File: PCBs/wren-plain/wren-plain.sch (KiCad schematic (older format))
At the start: 68 parts, among them J1 TRRS_Jack, SW0 Reset, U1 Elite-C

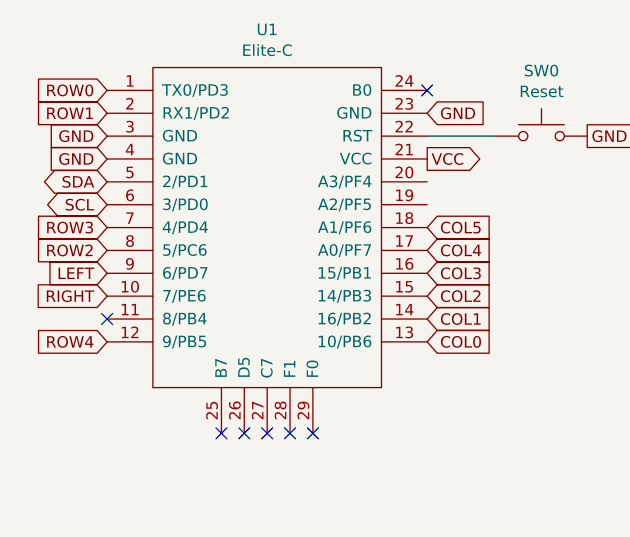
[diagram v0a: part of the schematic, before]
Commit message: Standardize MCU Pins
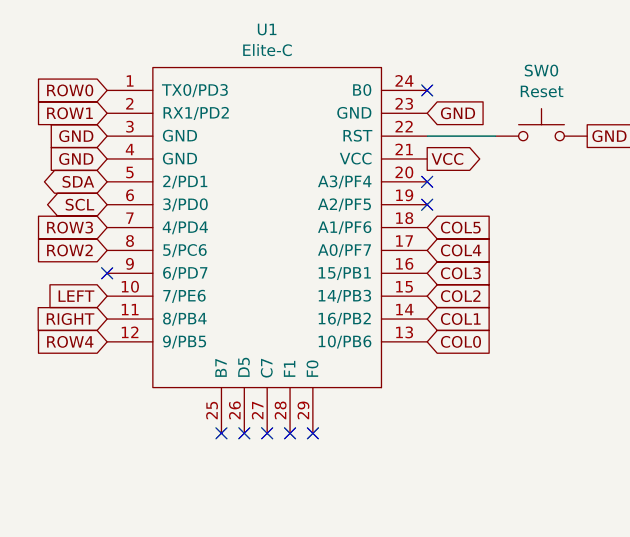
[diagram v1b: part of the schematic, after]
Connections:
- net LEFT: now also U1.10 (7/PE6); no longer U1.9 (6/PD7)
- net RIGHT: now also U1.11 (8/PB4); no longer U1.10 (7/PE6)
- no-connect marks 7 -> 9
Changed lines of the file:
@@
 Text GLabel 1800 2550 0    50   Input ~ 0
 ROW4
-NoConn ~ 1800 2450
 $Comp
 L Device:R_Small R2
@@
 	1    0    0    -1
 $EndComp
-Text GLabel 1800 2250 0    50   Input ~ 0
+Text GLabel 1800 2350 0    50   Input ~ 0
 LEFT
-Text GLabel 1800 2350 0    50   Input ~ 0
+Text GLabel 1800 2450 0    50   Input ~ 0
 RIGHT
 NoConn ~ 2300 2950
@@
 NoConn ~ 2600 2950
 NoConn ~ 2700 2950
+NoConn ~ 3200 1850
+NoConn ~ 3200 1950
+NoConn ~ 1800 2250
 $EndSCHEMATC
